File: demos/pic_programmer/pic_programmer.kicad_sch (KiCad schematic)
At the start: 56 parts, among them J1 DB9-FEMAL, P1 CONN_2, P101 CONN_1, P102 CONN_1, P103 CONN_1, P104 CONN_1, P105 CONN_1, P106 CONN_1, Q1 BC237, Q2 BC307, Q3 BC307, U2 74HC125, U3 7805, U4 LT1373

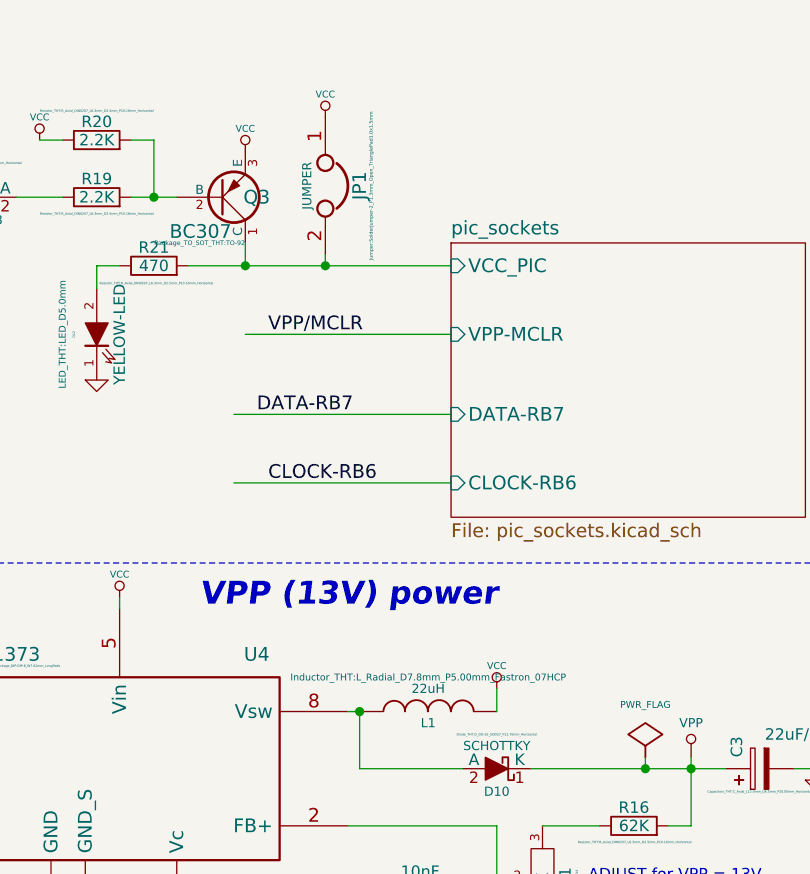
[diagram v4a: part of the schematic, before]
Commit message: Demos: update to last changes in file format.
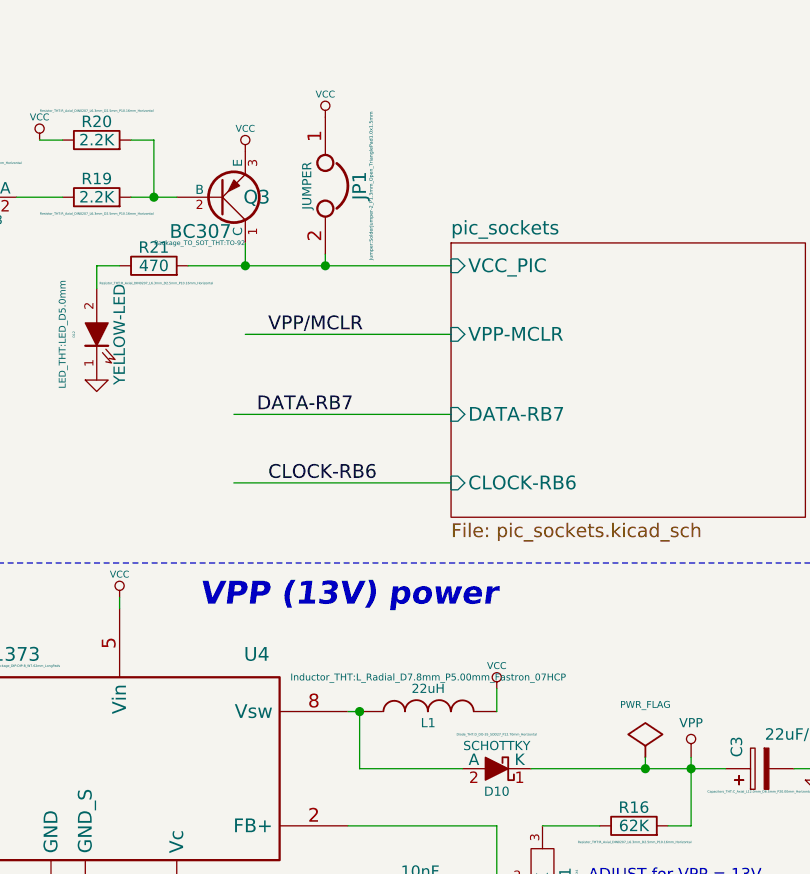
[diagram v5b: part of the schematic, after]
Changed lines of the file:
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@@
     (stroke (width 0) (type solid) (color 0 0 0 0))
     (fill (color 0 0 0 0.0000))
-    (property "Nom feuille" "pic_sockets" (id 0) (at 233.68 77.9775 0)
+    (property "Sheet name" "pic_sockets" (id 0) (at 233.68 77.9775 0)
       (effects (font (size 1.524 1.524)) (justify left bottom))
     )
-    (property "Fichier de feuille" "pic_sockets.kicad_sch" (id 1) (at 233.68 109.8301 0)
+    (property "Sheet file" "pic_sockets.kicad_sch" (id 1) (at 233.68 109.8301 0)
       (effects (font (size 1.524 1.524)) (justify left top))
     )

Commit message: Demos update
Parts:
- added U (x3): (no value), symbol pic_programmer_schlib:VPP
- U: renamed from J1; value DB9-FEMAL -> (none); footprint Connector_Dsub:DSUB-9_Female_Horizontal_P2.77x2.84mm_EdgePinOffset7.70mm_Housed_MountingHolesOffset9.12mm -> (none)
- U: renamed from U2; value 74HC125 -> (none); footprint Package_DIP:DIP-14_W7.62mm_LongPads -> (none)
- U: renamed from R1; value 10K -> (none); footprint Resistor_THT:R_Axial_DIN0207_L6.3mm_D2.5mm_P10.16mm_Horizontal -> (none)
- U: renamed from R2; value 10K -> (none); footprint Resistor_THT:R_Axial_DIN0207_L6.3mm_D2.5mm_P10.16mm_Horizontal -> (none)
- U: renamed from D2; value BAT43 -> (none); footprint Diode_THT:D_DO-35_SOD27_P7.62mm_Horizontal -> (none)
- U: renamed from D3; value BAT43 -> (none); footprint Diode_THT:D_DO-35_SOD27_P7.62mm_Horizontal -> (none)
- U: renamed from R3; value 10K -> (none); footprint Resistor_THT:R_Axial_DIN0207_L6.3mm_D2.5mm_P10.16mm_Horizontal -> (none)
- U: renamed from R4; value 10K -> (none); footprint Resistor_THT:R_Axial_DIN0207_L6.3mm_D2.5mm_P10.16mm_Horizontal -> (none)
- U: renamed from D4; value BAT43 -> (none); footprint Diode_THT:D_DO-35_SOD27_P7.62mm_Horizontal -> (none)
- U: renamed from D5; value BAT43 -> (none); footprint Diode_THT:D_DO-35_SOD27_P7.62mm_Horizontal -> (none)
- U: renamed from R5; value 10K -> (none); footprint Resistor_THT:R_Axial_DIN0207_L6.3mm_D2.5mm_P10.16mm_Horizontal -> (none)
- U: renamed from R6; value 10K -> (none); footprint Resistor_THT:R_Axial_DIN0207_L6.3mm_D2.5mm_P10.16mm_Horizontal -> (none)
- U: renamed from D6; value BAT43 -> (none); footprint Diode_THT:D_DO-35_SOD27_P7.62mm_Horizontal -> (none)
- U: renamed from D7; value BAT43 -> (none); footprint Diode_THT:D_DO-35_SOD27_P7.62mm_Horizontal -> (none)
- U: renamed from R12; value 470 -> (none); footprint Resistor_THT:R_Axial_DIN0207_L6.3mm_D2.5mm_P10.16mm_Horizontal -> (none)
- U: renamed from R13; value 470 -> (none); footprint Resistor_THT:R_Axial_DIN0207_L6.3mm_D2.5mm_P10.16mm_Horizontal -> (none)
- U: renamed from R8; value 1K -> (none); footprint Resistor_THT:R_Axial_DIN0207_L6.3mm_D2.5mm_P10.16mm_Horizontal -> (none)
- U: renamed from Q1; value BC237 -> (none); footprint Package_TO_SOT_THT:TO-92 -> (none)
- U: renamed from R11; value 22K -> (none); footprint Resistor_THT:R_Axial_DIN0207_L6.3mm_D2.5mm_P10.16mm_Horizontal -> (none)
- U: renamed from R7; value 10K -> (none); footprint Resistor_THT:R_Axial_DIN0207_L6.3mm_D2.5mm_P10.16mm_Horizontal -> (none)
- U: renamed from Q2; value BC307 -> (none); footprint Package_TO_SOT_THT:TO-92 -> (none)
- U: renamed from R9; value 2.2K -> (none); footprint Resistor_THT:R_Axial_DIN0207_L6.3mm_D2.5mm_P10.16mm_Horizontal -> (none)
- U: renamed from D8; value RED-LED -> (none); footprint LED_THT:LED_D5.0mm -> (none)
- U: renamed from P1; value CONN_2 -> (none); footprint TerminalBlock_Altech:Altech_AK300_1x02_P5.00mm_45-Degree -> (none)
- U: renamed from D1; value 1N4004 -> (none); footprint Diode_THT:D_DO-35_SOD27_P12.70mm_Horizontal -> (none)
- U: renamed from C2; value 220uF -> (none); footprint Capacitor_THT:CP_Axial_L18.0mm_D6.5mm_P25.00mm_Horizontal -> (none)
- U: renamed from C1; value 100µF -> (none); footprint Capacitor_THT:CP_Axial_L18.0mm_D6.5mm_P25.00mm_Horizontal -> (none)
- U: renamed from R14; value 470 -> (none); footprint Resistor_THT:R_Axial_DIN0207_L6.3mm_D2.5mm_P10.16mm_Horizontal -> (none)
- U: renamed from D9; value GREEN-LED -> (none); footprint LED_THT:LED_D5.0mm -> (none)
- U: renamed from R17; value 22K -> (none); footprint Resistor_THT:R_Axial_DIN0207_L6.3mm_D2.5mm_P10.16mm_Horizontal -> (none)
- U: renamed from L1; value 22uH -> (none); footprint Inductor_THT:L_Radial_D7.8mm_P5.00mm_Fastron_07HCP -> (none)
- U: renamed from C3; value 22uF/25V -> (none); footprint Capacitors_THT:C_Axial_L12.0mm_D6.5mm_P20.00mm_Horizontal -> (none)
- U: renamed from C5; value 10nF -> (none); footprint Capacitor_THT:C_Disc_D5.1mm_W3.2mm_P5.00mm -> (none)
- U: renamed from R15; value 6.2K -> (none); footprint Resistor_THT:R_Axial_DIN0207_L6.3mm_D2.5mm_P10.16mm_Horizontal -> (none)
- U: renamed from R16; value 62K -> (none); footprint Resistor_THT:R_Axial_DIN0207_L6.3mm_D2.5mm_P10.16mm_Horizontal -> (none)
- U: renamed from U4; value LT1373 -> (none); footprint Package_DIP:DIP-8_W7.62mm_LongPads -> (none)
- U: renamed from C4; value 0 -> (none); footprint Capacitor_THT:C_Disc_D5.1mm_W3.2mm_P5.00mm -> (none)
- U: renamed from R10; value 5,1K -> (none); footprint Resistor_THT:R_Axial_DIN0207_L6.3mm_D2.5mm_P10.16mm_Horizontal -> (none)
- U: renamed from D10; value SCHOTTKY -> (none); footprint Diode_THT:D_DO-35_SOD27_P12.70mm_Horizontal -> (none)
- U: renamed from R18; value 220 -> (none); footprint Resistor_THT:R_Axial_DIN0207_L6.3mm_D2.5mm_P10.16mm_Horizontal -> (none)
- U: renamed from RV1; value 1K -> (none); footprint footprints:RV2X4 -> (none)
- U: renamed from Q3; value BC307 -> (none); footprint Package_TO_SOT_THT:TO-92 -> (none)
- U: renamed from R19; value 2.2K -> (none); footprint Resistor_THT:R_Axial_DIN0207_L6.3mm_D2.5mm_P10.16mm_Horizontal -> (none)
- U: renamed from R20; value 2.2K -> (none); footprint Resistor_THT:R_Axial_DIN0207_L6.3mm_D2.5mm_P10.16mm_Horizontal -> (none)
- U: renamed from R21; value 470 -> (none); footprint Resistor_THT:R_Axial_DIN0207_L6.3mm_D2.5mm_P10.16mm_Horizontal -> (none)
- U: renamed from D12; value YELLOW-LED -> (none); footprint LED_THT:LED_D5.0mm -> (none)
- U: renamed from D11; value BAT43 -> (none); footprint Diode_THT:D_DO-35_SOD27_P7.62mm_Horizontal -> (none)
- U: renamed from JP1; value JUMPER -> (none); footprint Jumper:SolderJumper-2_P1.3mm_Open_TrianglePad1.0x1.5mm -> (none)
- U: renamed from C9; value 220nF -> (none); footprint Capacitor_THT:C_Disc_D5.1mm_W3.2mm_P5.00mm -> (none)
- U: renamed from P101; value CONN_1 -> (none); footprint MountingHole:MountingHole_4.3mm_M4 -> (none)
- U: renamed from P102; value CONN_1 -> (none); footprint MountingHole:MountingHole_4.3mm_M4 -> (none)
- U: renamed from P103; value CONN_1 -> (none); footprint MountingHole:MountingHole_4.3mm_M4 -> (none)
- U: renamed from P104; value CONN_1 -> (none); footprint MountingHole:MountingHole_4.3mm_M4 -> (none)
- U: renamed from P105; value CONN_1 -> (none); footprint MountingHole:MountingHole_4.3mm_M4 -> (none)
- U: renamed from P106; value CONN_1 -> (none); footprint MountingHole:MountingHole_4.3mm_M4 -> (none)
- U: renamed from U3; value 7805 -> (none); footprint Package_TO_SOT_THT:TO-220-3_Horizontal_TabDown -> (none)
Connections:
- net DATA-RB7: now also U.2; no longer U.12
- net GND: now also U.1, U.1, U.1; no longer U.10, U.13, U.4
- net PC-DATA-IN: now also U.3; no longer U.11
- net VPP: now also U.1 (VPP), U.1 (VPP), U.1 (VPP)
- net at U.1 (K), U.2, U.2 (A): now also U.2; no longer U.5
- net at U.1: now also U.3; no longer U.6
- net at U.1: now also U.3; no longer U.8
- net at U.1 (K), U.2, U.2 (A): now also U.2; no longer U.9

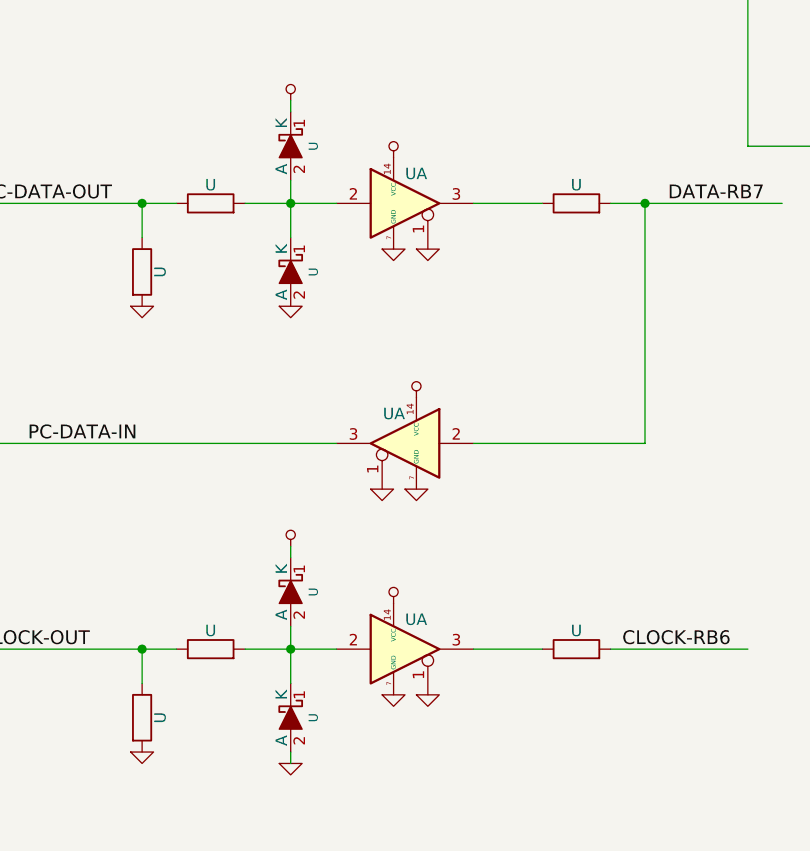
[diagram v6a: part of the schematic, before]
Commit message: demo: a minor fix in symbol lib.
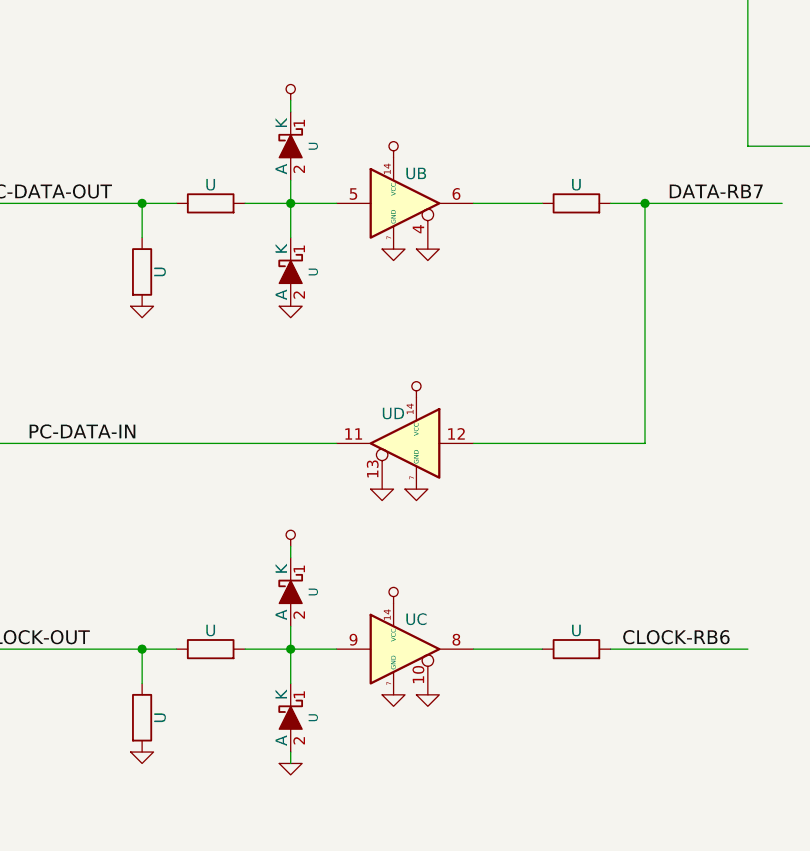
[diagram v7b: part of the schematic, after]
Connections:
- net DATA-RB7: now also U.12; no longer U.2
- net GND: now also U.10, U.13, U.4; no longer U.1, U.1, U.1
- net PC-DATA-IN: now also U.11; no longer U.3
- net at U.1 (K), U.2, U.2 (A): now also U.5; no longer U.2
- net at U.1: now also U.6; no longer U.3
- net at U.1 (K), U.2, U.2 (A): now also U.9; no longer U.2
- net at U.1: now also U.8; no longer U.3
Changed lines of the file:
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@@
-(kicad_sch (version 20220404) (generator eeschema)
+(kicad_sch (version 20220904) (generator eeschema)
   (paper "A4")
   (title_block
@@
     (pin "1")
   )
-  (symbol (lib_id "pic_programmer_schlib:74LS125") (at 110.49 80.01 0) (unit 1)
+  (symbol (lib_id "pic_programmer_schlib:74LS125") (at 110.49 80.01 0) (unit 2)
     (in_bom yes) (on_board yes)
     (default_instance (reference "U") (unit 1) (value "") (footprint ""))
@@
     (pin "1")
   )
-  (symbol (lib_id "pic_programmer_schlib:74LS125") (at 110.49 129.54 0) (unit 1)
+  (symbol (lib_id "pic_programmer_schlib:74LS125") (at 110.49 129.54 0) (unit 3)
     (in_bom yes) (on_board yes)
     (default_instance (reference "U") (unit 1) (value "") (footprint ""))
@@
     (pin "1")
   )
-  (symbol (lib_id "pic_programmer_schlib:74LS125") (at 110.49 106.68 0) (mirror y) (unit 1)
-    (in_bom yes) (on_board yes)
-    (default_instance (reference "U") (unit 1) (value "") (footprint ""))
+  (symbol (lib_id "pic_programmer_schlib:74LS125") (at 110.49 106.68 0) (mirror y) (unit 4)
+    (in_bom yes) (on_board yes)
+    (default_instance (reference "U") (unit 1) (value "") (footprint ""))
